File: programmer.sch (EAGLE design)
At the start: 17 parts, among them IC1 MIC5225-3.3v, Q1 BSS138, Q2 BSS138, Q3 BSS138, Q4 BSS138

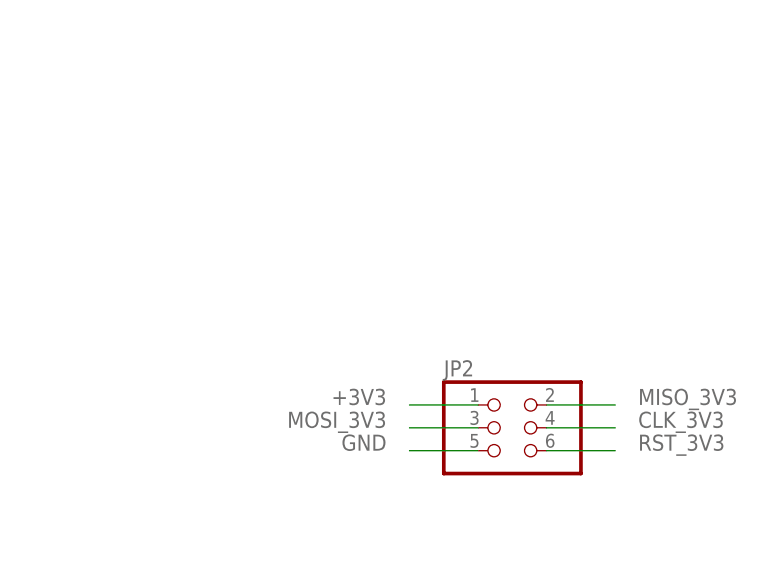
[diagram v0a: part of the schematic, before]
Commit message: Migrate to EAGLE v9.0.1
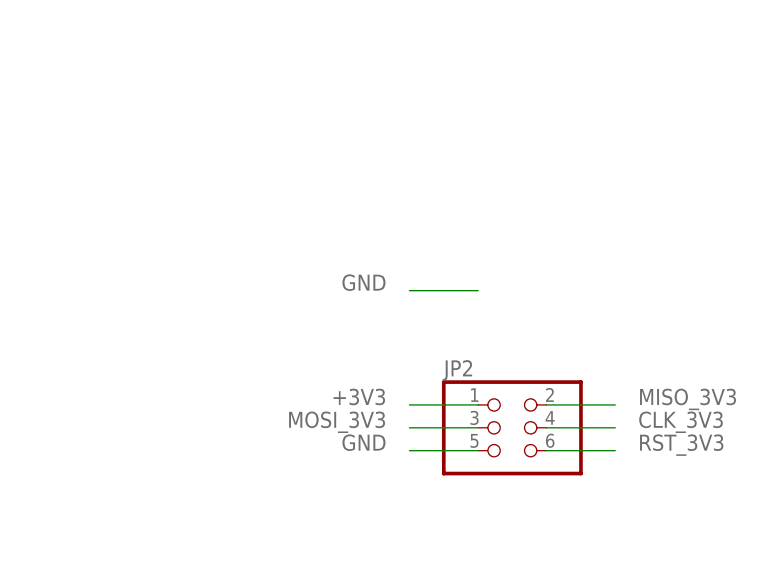
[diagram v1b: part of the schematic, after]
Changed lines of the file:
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@@
 <?xml version="1.0" encoding="utf-8"?>
 <!DOCTYPE eagle SYSTEM "eagle.dtd">
-<eagle version="7.7.0">
+<eagle version="9.0.1">
 <drawing>
 <settings>
@@
 <label x="139.7" y="78.74" size="1.778" layer="95" rot="R270"/>
 </segment>
+<segment>
+<pinref part="PAD5" gate="G$1" pin="P"/>
+<wire x1="208.28" y1="76.2" x2="200.66" y2="76.2" width="0.1524" layer="91"/>
+<label x="198.12" y="76.2" size="1.778" layer="95" rot="MR0"/>
+</segment>
 </net>
 </nets>
@@
 </schematic>
 </drawing>
+<compatibility>
+<note version="8.2" severity="warning">
+Since Version 8.2, EAGLE supports online libraries. The ids
+of those online libraries will not be understood (or retained)
+with this version.
+</note>
+<note version="8.3" severity="warning">
+Since Version 8.3, EAGLE supports URNs for individual library
+assets (packages, symbols, and devices). The URNs of those assets
+will not be understood (or retained) with this version.
+</note>
+<note version="8.3" severity="warning">
+Since Version 8.3, EAGLE supports the association of 3D packages
+with devices in libraries, schematics, and board files. Those 3D
+packages will not be understood (or retained) with this version.
+</note>
+</compatibility>
 </eagle>

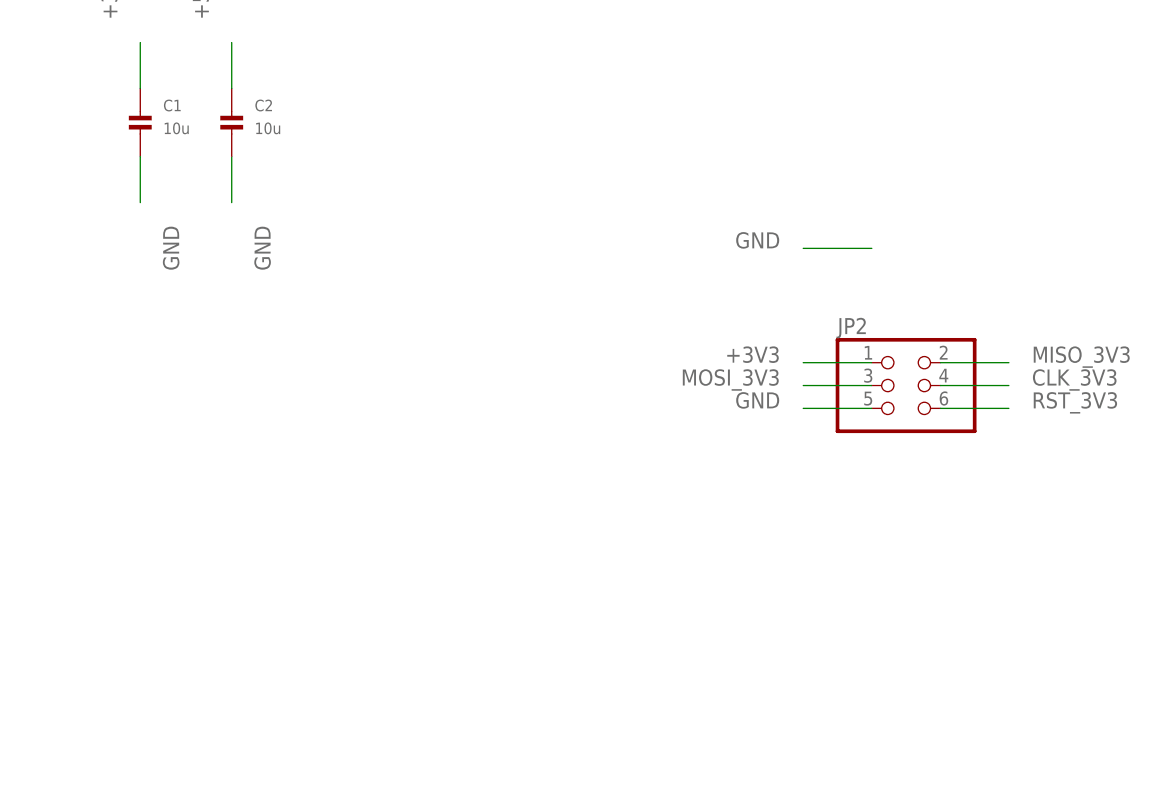
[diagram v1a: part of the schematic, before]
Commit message: Update ATtiny programming interface board
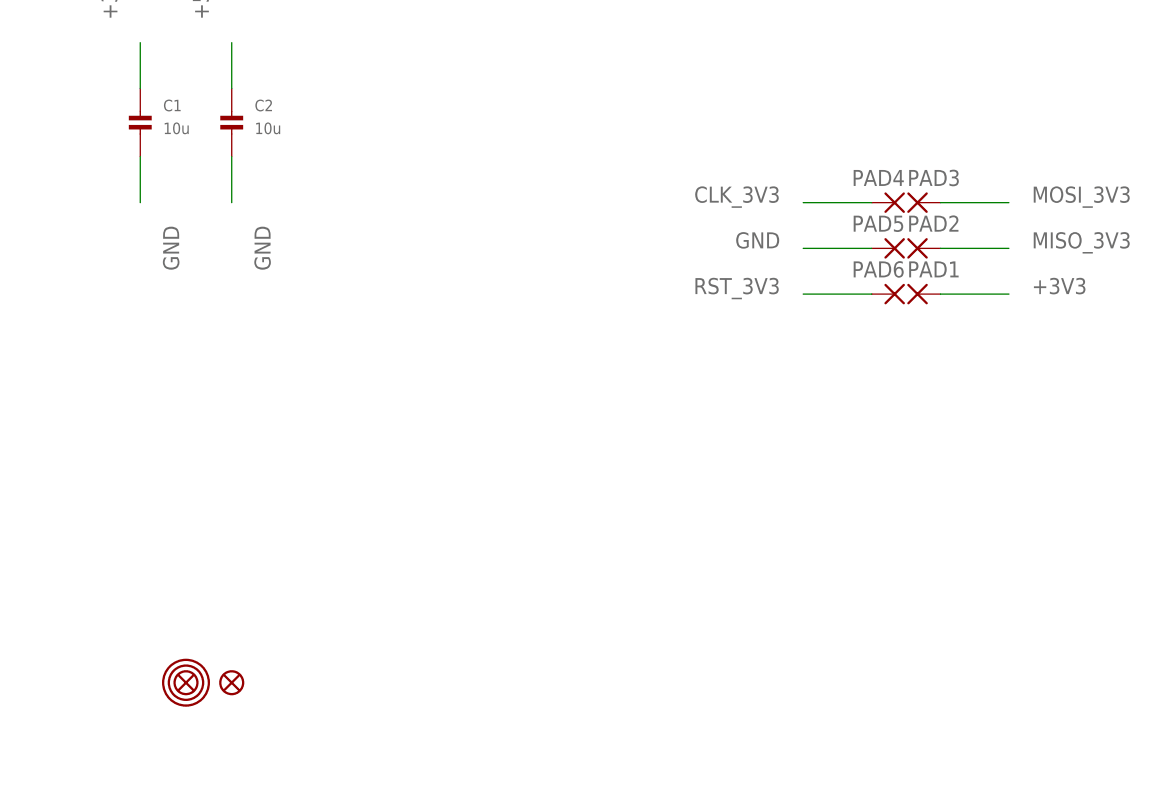
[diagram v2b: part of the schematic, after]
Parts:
- removed JP2: (no value), microbuilder:HEADER-2X3
- added FID1, FID2: FIDUCIAL1X2.5, microbuilder:FIDUCIAL1X2.5
- added PAD1, PAD2, PAD3, PAD4, PAD5, PAD6: WIREPADSMD1,27-254, wirepad:WIREPADSMD1,27-254
- added U$1: MOUNTINGHOLE2.5, microbuilder:MOUNTINGHOLE2.5
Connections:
- net +3V3: now also PAD1.P; no longer JP2.1
- net CLK_3V3: now also PAD4.P; no longer JP2.4
- net GND: now also PAD5.P; no longer JP2.5
- net MISO_3V3: now also PAD2.P; no longer JP2.2
- net MOSI_3V3: now also PAD3.P; no longer JP2.3
- net RST_3V3: now also PAD6.P; no longer JP2.6
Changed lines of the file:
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@@
 <settings>
 <setting alwaysvectorfont="yes"/>
+<setting keepoldvectorfont="yes"/>
 <setting verticaltext="up"/>
 </settings>
@@
 <part name="IC1" library="adafruit" deviceset="LP298X" device="S" value="MIC5225-3.3v"/>
 <part name="JP1" library="microbuilder" deviceset="HEADER-1X6" device="ROUND"/>
-<part name="JP2" library="microbuilder" deviceset="HEADER-2X3" device=""/>
 <part name="C1" library="microbuilder" deviceset="CAP_CERAMIC" device="0603" value="10u"/>
 <part name="C2" library="microbuilder" deviceset="CAP_CERAMIC" device="0603" value="10u"/>
+<part name="PAD1" library="wirepad" library_urn="urn:adsk.eagle:library:412" deviceset="WIREPAD" device="SMD1,27-254" package3d_urn="urn:adsk.eagle:package:30839/1"/>
+<part name="PAD2" library="wirepad" library_urn="urn:adsk.eagle:library:412" deviceset="WIREPAD" device="SMD1,27-254" package3d_urn="urn:adsk.eagle:package:30839/1"/>
+<part name="PAD3" library="wirepad" library_urn="urn:adsk.eagle:library:412" deviceset="WIREPAD" device="SMD1,27-254" package3d_urn="urn:adsk.eagle:package:30839/1"/>
+<part name="PAD4" library="wirepad" library_urn="urn:adsk.eagle:library:412" deviceset="WIREPAD" device="SMD1,27-254" package3d_urn="urn:adsk.eagle:package:30839/1"/>
+<part name="PAD5" library="wirepad" library_urn="urn:adsk.eagle:library:412" deviceset="WIREPAD" device="SMD1,27-254" package3d_urn="urn:adsk.eagle:package:30839/1"/>
+<part name="PAD6" library="wirepad" library_urn="urn:adsk.eagle:library:412" deviceset="WIREPAD" device="SMD1,27-254" package3d_urn="urn:adsk.eagle:package:30839/1"/>
+<part name="FID1" library="microbuilder" deviceset="FIDUCIAL" device="1X2.5"/>
+<part name="FID2" library="microbuilder" deviceset="FIDUCIAL" device="1X2.5"/>
+<part name="U$1" library="microbuilder" deviceset="MOUNTINGHOLE" device="2.5"/>
 </parts>
 <sheets>
@@
 <instance part="IC1" gate="G$1" x="71.12" y="88.9" rot="R270"/>
 <instance part="JP1" gate="A" x="76.2" y="25.4"/>
-<instance part="JP2" gate="G$1" x="213.36" y="60.96"/>
 <instance part="C1" gate="G$1" x="127" y="88.9"/>
 <instance part="C2" gate="G$1" x="137.16" y="88.9"/>
+<instance part="PAD1" gate="G$1" x="213.36" y="71.12" smashed="yes">
+<attribute name="NAME" x="212.217" y="72.9742" size="1.778" layer="95"/>
+</instance>
+<instance part="PAD2" gate="G$1" x="213.36" y="76.2" smashed="yes">
+<attribute name="NAME" x="212.217" y="78.0542" size="1.778" layer="95"/>
+</instance>
+<instance part="PAD3" gate="G$1" x="213.36" y="81.28" smashed="yes">
+<attribute name="NAME" x="212.217" y="83.1342" size="1.778" layer="95"/>
+</instance>
+<instance part="PAD4" gate="G$1" x="210.82" y="81.28" smashed="yes" rot="MR0">
+<attribute name="NAME" x="211.963" y="83.1342" size="1.778" layer="95" rot="MR0"/>
+</instance>
+<instance part="PAD5" gate="G$1" x="210.82" y="76.2" smashed="yes" rot="MR0">
+<attribute name="NAME" x="211.963" y="78.0542" size="1.778" layer="95" rot="MR0"/>
+</instance>
+<instance part="PAD6" gate="G$1" x="210.82" y="71.12" smashed="yes" rot="MR0">
+<attribute name="NAME" x="211.963" y="72.9742" size="1.778" layer="95" rot="MR0"/>
+</instance>
+<instance part="FID1" gate="G$1" x="132.08" y="27.94"/>
+<instance part="FID2" gate="G$1" x="137.16" y="27.94" rot="MR0"/>
+<instance part="U$1" gate="G$1" x="132.08" y="27.94"/>
 </instances>
 <busses>
@@
 </segment>
 <segment>
-<pinref part="JP2" gate="G$1" pin="1"/>
-<wire x1="208.28" y1="63.5" x2="200.66" y2="63.5" width="0.1524" layer="91"/>
-<label x="198.12" y="63.5" size="1.778" layer="95" rot="MR0"/>
-</segment>
-<segment>
 <pinref part="C1" gate="G$1" pin="P$1"/>
 <wire x1="127" y1="93.98" x2="127" y2="99.06" width="0.1524" layer="91"/>
 <label x="124.46" y="101.6" size="1.778" layer="95" rot="R90"/>
+</segment>
+<segment>
+<pinref part="PAD1" gate="G$1" pin="P"/>
+<wire x1="215.9" y1="71.12" x2="223.52" y2="71.12" width="0.1524" layer="91"/>
+<label x="226.06" y="71.12" size="1.778" layer="95"/>
 </segment>
 </net>
@@
 </segment>
 <segment>
-<pinref part="JP2" gate="G$1" pin="2"/>
-<wire x1="215.9" y1="63.5" x2="223.52" y2="63.5" width="0.1524" layer="91"/>
-<label x="226.06" y="63.5" size="1.778" layer="95"/>
+<pinref part="PAD2" gate="G$1" pin="P"/>
+<wire x1="215.9" y1="76.2" x2="223.52" y2="76.2" width="0.1524" layer="91"/>
+<label x="226.06" y="76.2" size="1.778" layer="95"/>
 </segment>
 </net>
@@
 </segment>
 <segment>
-<pinref part="JP2" gate="G$1" pin="3"/>
-<wire x1="208.28" y1="60.96" x2="200.66" y2="60.96" width="0.1524" layer="91"/>
-<label x="198.12" y="60.96" size="1.778" layer="95" rot="MR0"/>
+<pinref part="PAD3" gate="G$1" pin="P"/>
+<wire x1="215.9" y1="81.28" x2="223.52" y2="81.28" width="0.1524" layer="91"/>
+<label x="226.06" y="81.28" size="1.778" layer="95"/>
 </segment>
 </net>
@@
 </segment>
 <segment>
-<pinref part="JP2" gate="G$1" pin="6"/>
-<wire x1="215.9" y1="58.42" x2="223.52" y2="58.42" width="0.1524" layer="91"/>
-<label x="226.06" y="58.42" size="1.778" layer="95"/>
+<pinref part="PAD6" gate="G$1" pin="P"/>
+<wire x1="208.28" y1="71.12" x2="200.66" y2="71.12" width="0.1524" layer="91"/>
+<label x="198.12" y="71.12" size="1.778" layer="95" rot="MR0"/>
 </segment>
 </net>
@@
 </segment>
 <segment>
-<pinref part="JP2" gate="G$1" pin="4"/>
-<wire x1="215.9" y1="60.96" x2="223.52" y2="60.96" width="0.1524" layer="91"/>
-<label x="226.06" y="60.96" size="1.778" layer="95"/>
+<pinref part="PAD4" gate="G$1" pin="P"/>
+<wire x1="208.28" y1="81.28" x2="200.66" y2="81.28" width="0.1524" layer="91"/>
+<label x="198.12" y="81.28" size="1.778" layer="95" rot="MR0"/>
 </segment>
 </net>
@@
 </segment>
 <segment>
-<pinref part="JP2" gate="G$1" pin="5"/>
-<wire x1="208.28" y1="58.42" x2="200.66" y2="58.42" width="0.1524" layer="91"/>
-<label x="198.12" y="58.42" size="1.778" layer="95" rot="MR0"/>
-</segment>
-<segment>
